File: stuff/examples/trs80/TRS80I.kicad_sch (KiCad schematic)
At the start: 74 parts, among them U5 4023, U6 4023

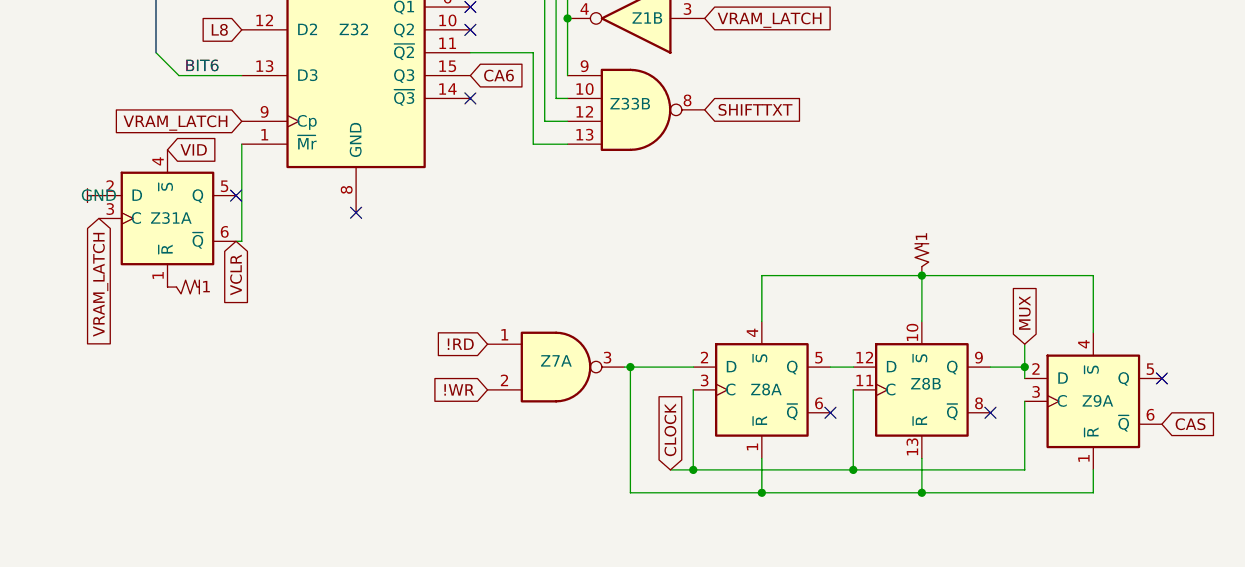
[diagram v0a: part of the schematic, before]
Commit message: Fis RS pins in DCTrigger Use Optimiser for DCTrigger pins in case of no R/S pins
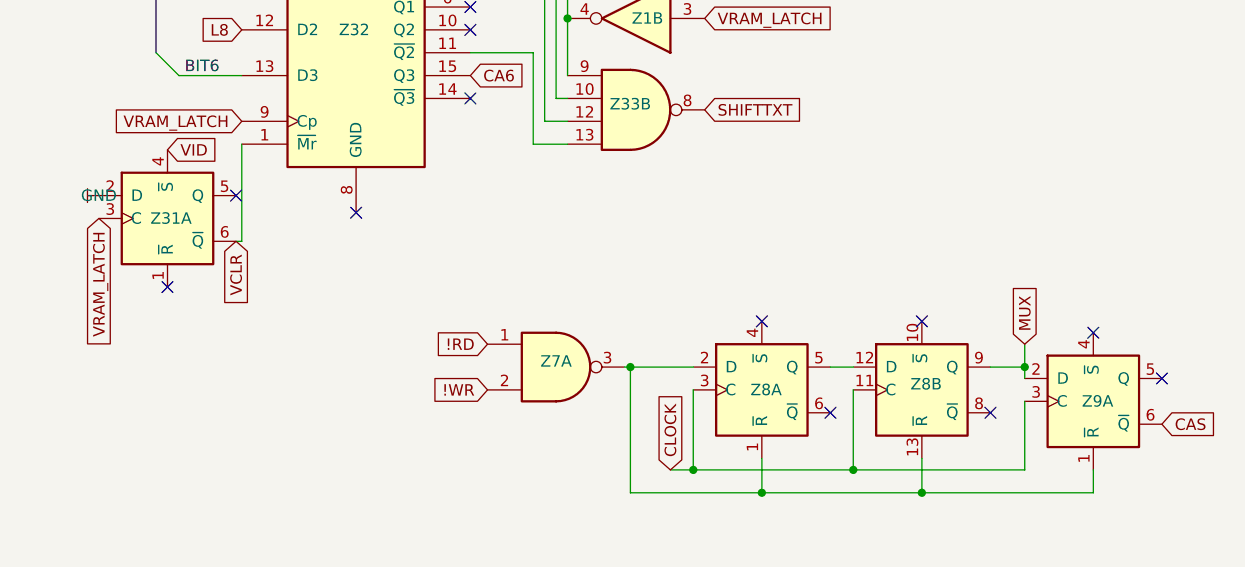
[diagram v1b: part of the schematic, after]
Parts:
- removed pullup30, pullup9: pull_up, symbol chip:PULLUP
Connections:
- now unconnected: Z8.10 (~{S}), Z8.4 (~{S}), Z9.4 (~{S})
- no-connect marks 35 -> 39
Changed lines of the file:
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@@
   (junction (at 292.735 90.17) (diameter 0) (color 0 0 0 0)
   )
-  (junction (at 333.375 122.555) (diameter 0) (color 0 0 0 0)
-  )
   (junction (at 333.375 146.685) (diameter 0) (color 0 0 0 0)
   )
@@
   (junction (at 259.715 45.72) (diameter 0) (color 0 0 0 0)
   )
+  (no_connect (at 249.555 123.825))
   (no_connect (at 203.2 62.865))
   (no_connect (at 193.04 260.985))
@@
   (no_connect (at 340.995 137.795))
   (no_connect (at 152.4 44.45))
+  (no_connect (at 333.375 127.635))
+  (no_connect (at 352.425 128.905))
   (no_connect (at 203.2 65.405))
   (no_connect (at 283.21 92.71))
@@
   (no_connect (at 168.91 71.12))
   (no_connect (at 115.57 90.805))
+  (no_connect (at 315.595 127.635))
   (no_connect (at 107.95 170.18))
   (no_connect (at 168.91 68.58))
@@
     (stroke (width 0) (type default))
   )
-  (wire (pts (xy 352.425 128.905) (xy 352.425 122.555))
-    (stroke (width 0) (type default))
-  )
   (bus (pts (xy 132.08 25.4) (xy 132.08 27.94))
     (stroke (width 0) (type default))
@@
     (stroke (width 0) (type default))
   )
-  (wire (pts (xy 333.375 122.555) (xy 352.425 122.555))
-    (stroke (width 0) (type default))
-  )
   (wire (pts (xy 223.52 45.085) (xy 226.695 45.085))
     (stroke (width 0) (type default))
@@
     (stroke (width 0) (type default))
   )
-  (wire (pts (xy 315.595 122.555) (xy 315.595 127.635))
-    (stroke (width 0) (type default))
-  )
   (wire (pts (xy 241.3 43.18) (xy 241.935 43.18))
     (stroke (width 0) (type default))
@@
     (stroke (width 0) (type default))
   )
-  (wire (pts (xy 333.375 122.555) (xy 333.375 127.635))
-    (stroke (width 0) (type default))
-  )
   (wire (pts (xy 147.955 191.135) (xy 151.765 191.135))
     (stroke (width 0) (type default))
@@
     (stroke (width 0) (type default))
   )
-  (wire (pts (xy 315.595 122.555) (xy 333.375 122.555))
-    (stroke (width 0) (type default))
-  )
   (bus (pts (xy 231.775 30.48) (xy 231.775 57.15))
     (stroke (width 0) (type default))
@@
     )
   )
-  (symbol (lib_id "chip:PULLUP") (at 249.555 123.825 180) (unit 1)
-    (in_bom yes) (on_board yes) (dnp no)
-    (property "Reference" "pullup30" (at 249.555 121.285 0)
-      (effects (font (size 1.27 1.27)) hide)
-    )
-    (property "Value" "pull_up" (at 249.555 121.285 0)
-      (effects (font (size 1.27 1.27)) hide)
-    )
-    (property "Footprint" "" (at 249.555 123.825 0)
-      (effects (font (size 1.27 1.27)) hide)
-    )
-    (property "Datasheet" "" (at 249.555 123.825 0)
-      (effects (font (size 1.27 1.27)) hide)
-    )
-    (pin "1")
-    (instances
-      (project "TRS80I"
-        (path "/5810480a-4982-4194-abfa-f24d4210ea86"
-          (reference "pullup30") (unit 1)
-        )
-      )
-    )
-  )
   (symbol (lib_id "chip:PULLUP") (at 259.715 29.21 0) (mirror x) (unit 1)
     (in_bom yes) (on_board yes) (dnp no)
@@
         )
       )
-    )
-  )
-  (symbol (lib_id "chip:PULLUP") (at 333.375 122.555 270) (unit 1)
-    (in_bom yes) (on_board yes) (dnp no)
-    (property "Reference" "pullup9" (at 330.835 122.555 0)
-      (effects (font (size 1.27 1.27)) hide)
-    )
-    (property "Value" "pull_up" (at 330.835 122.555 0)
-      (effects (font (size 1.27 1.27)) hide)
-    )
-    (property "Footprint" "" (at 333.375 122.555 0)
-      (effects (font (size 1.27 1.27)) hide)
-    )
-    (property "Datasheet" "" (at 333.375 122.555 0)
-      (effects (font (size 1.27 1.27)) hide)
-    )
-    (pin "1")
-    (instances
-      (project "TRS80I"
-        (path "/5810480a-4982-4194-abfa-f24d4210ea86"
-          (reference "pullup9") (unit 1)
-        )
-      )

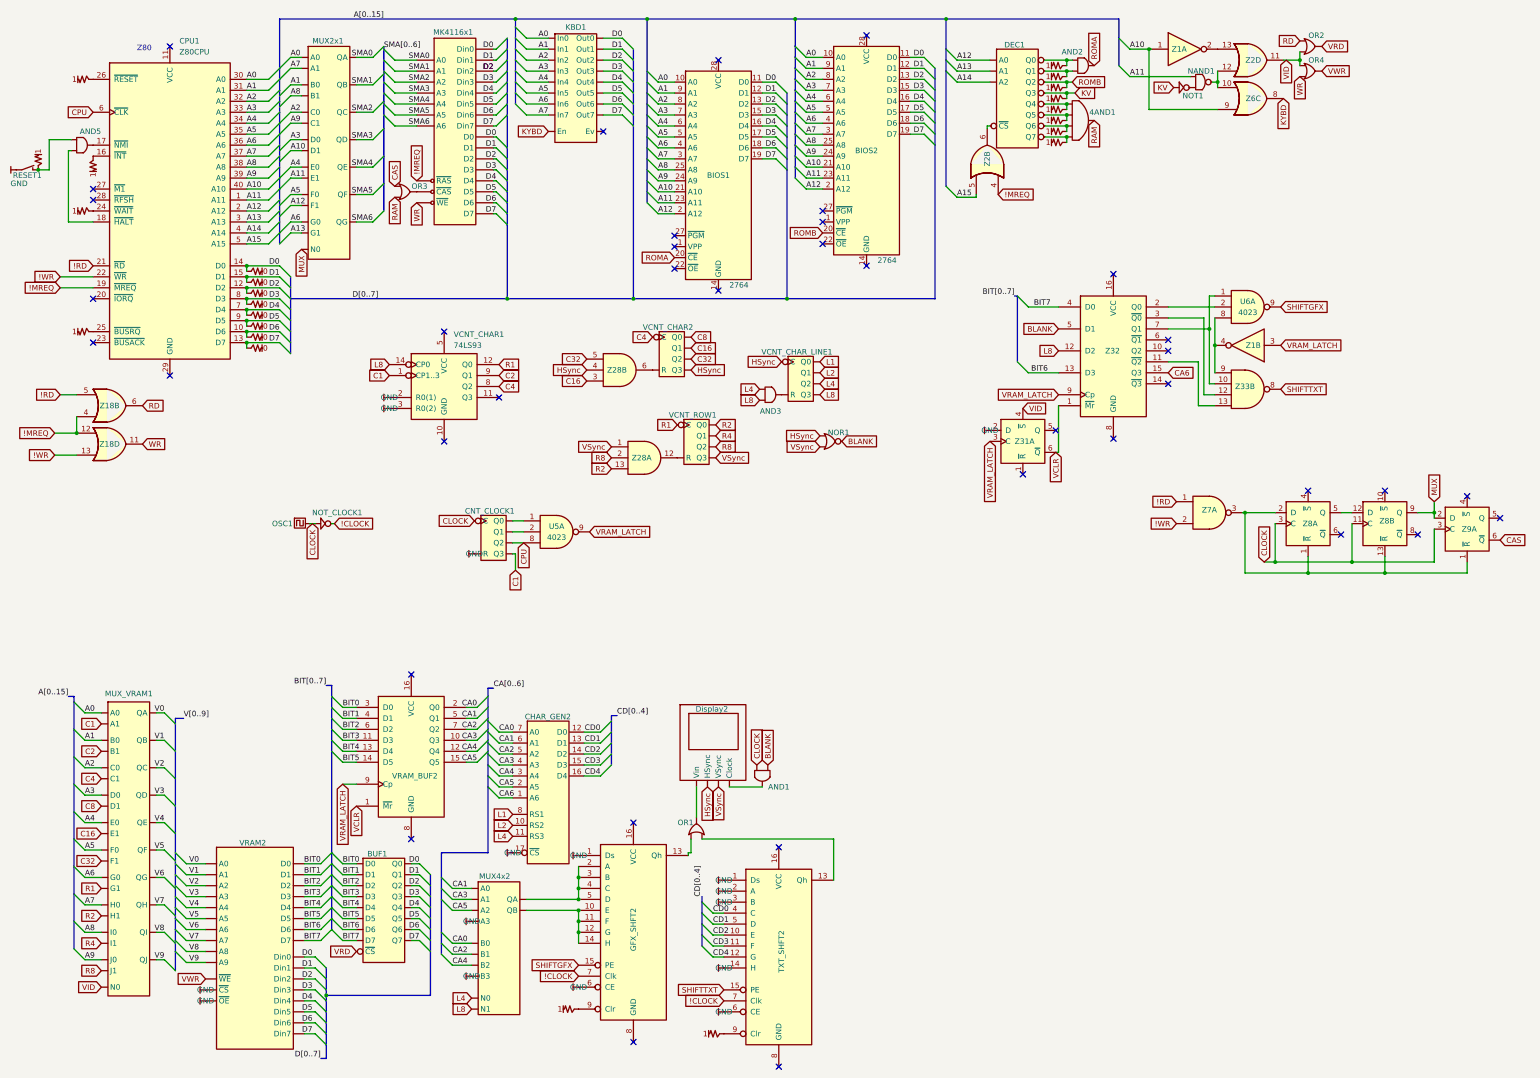
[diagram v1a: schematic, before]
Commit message: fix 74LS92 (It's not divider by 16, but rather by 12). Other fixes.
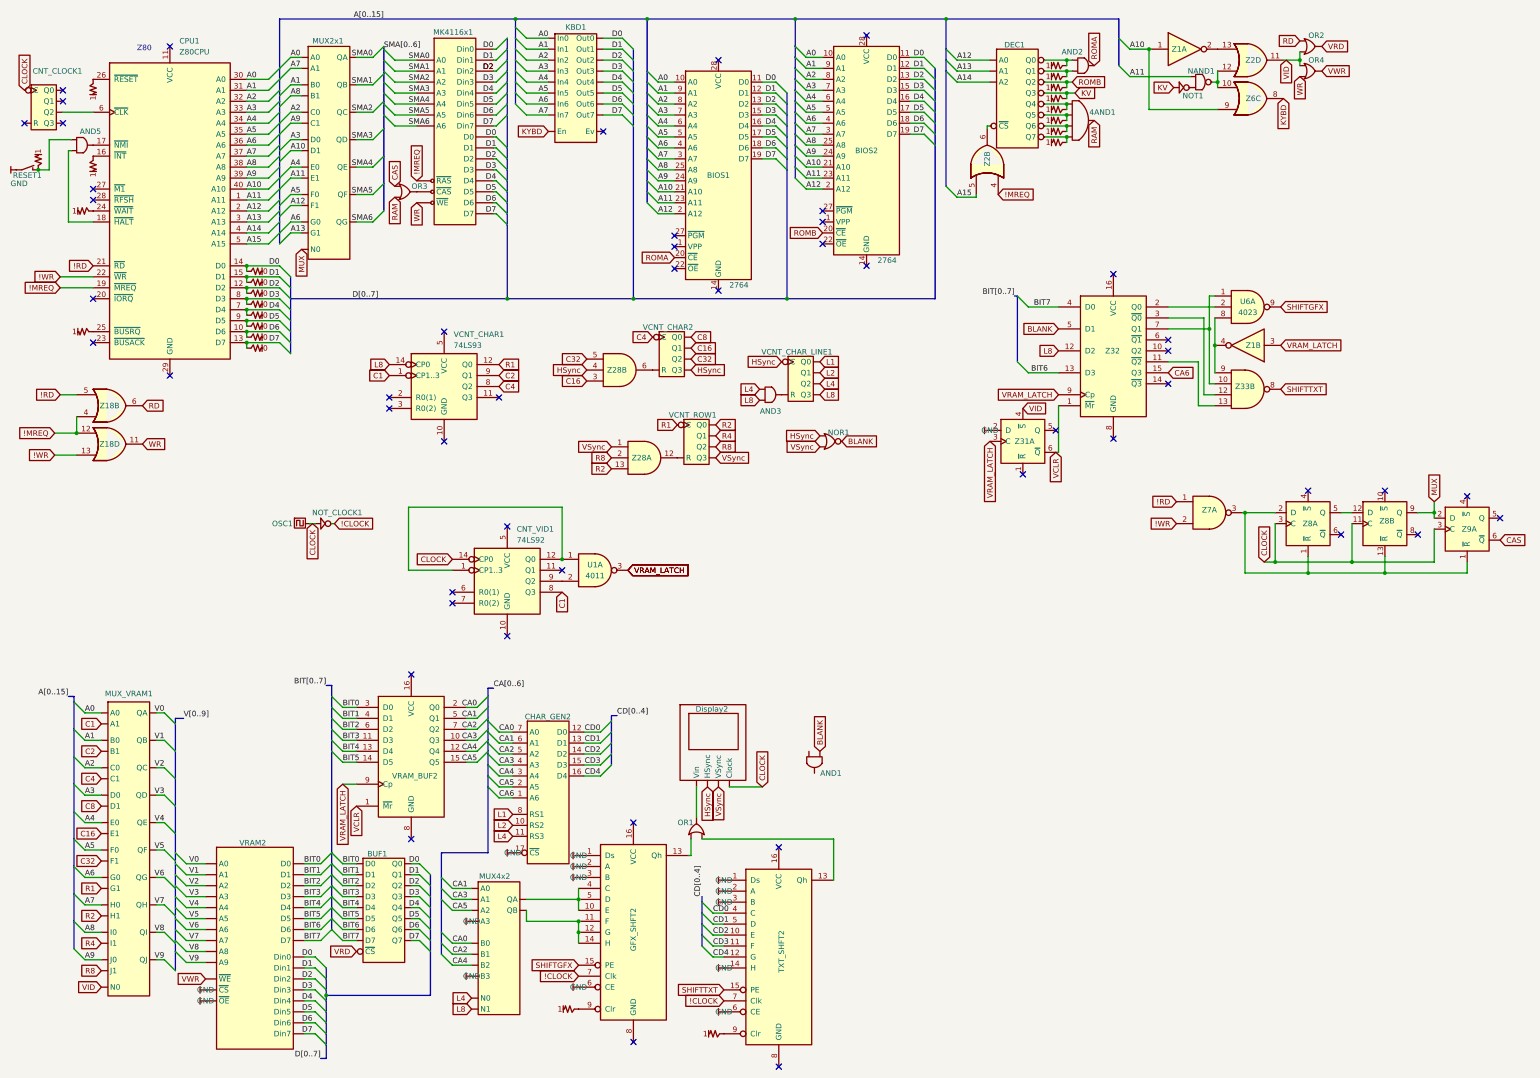
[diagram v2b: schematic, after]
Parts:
- removed U5: 4023, symbol 4xxx:4023
- added CNT_VID1: 74LS92, TRS80IUS:DIP-14_W7.62mm, symbol 74xx:74LS92
- added U1: 4011, symbol 4xxx:4011
- OSC1: SymPartParam start -> (none)
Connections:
- net C1: now also CNT_VID1.8 (Q3); no longer CNT_CLOCK1.5 (Q3)
- net CLOCK: now also Display2.1 (Clock), CNT_VID1.14 (CP0); no longer AND1.1 (IN0)
- net VRAM_LATCH: now also U1.3
- net gnd: now also GFX_SHFT2.2 (A), GFX_SHFT2.3 (B); no longer CNT_CLOCK1.1 (R), VCNT_CHAR1.2 (R0(1)), VCNT_CHAR1.3 (R0(2))
- net at AND1.3 (OUT): no longer Display2.1 (Clock)
- net at GFX_SHFT2.11 (F), GFX_SHFT2.12 (G), GFX_SHFT2.14 (H)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: no longer GFX_SHFT2.10 (E)
- net at GFX_SHFT2.4 (C), GFX_SHFT2.5 (D), MUX4x2.11 (QA): now also GFX_SHFT2.10 (E); no longer GFX_SHFT2.2 (A), GFX_SHFT2.3 (B)
- net CPU: no longer names the net of CNT_CLOCK1.4 (Q2), CPU1.6 (~{CLK})
- new net: CNT_VID1.1 (CP1..3), CNT_VID1.12 (Q0), U1.1
- new net: CNT_VID1.9 (Q2), U1.2
- no-connect marks 39 -> 50

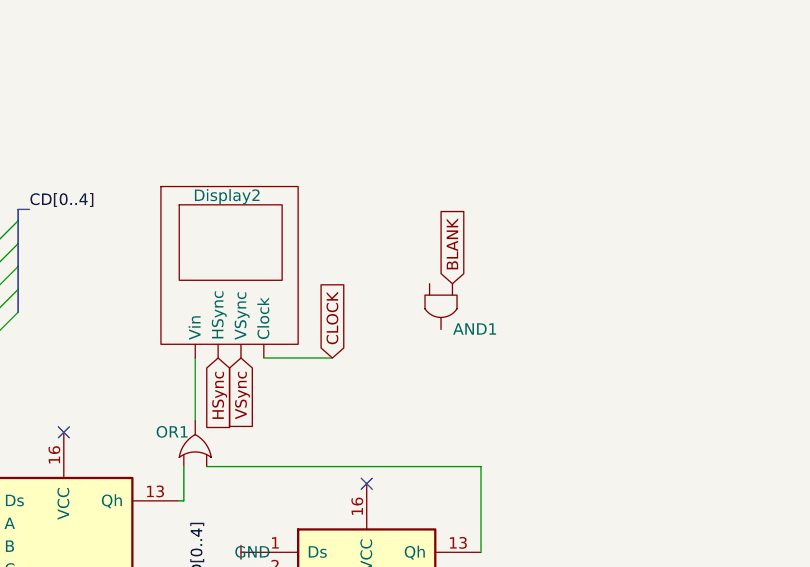
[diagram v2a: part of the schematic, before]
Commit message: Expand wire API
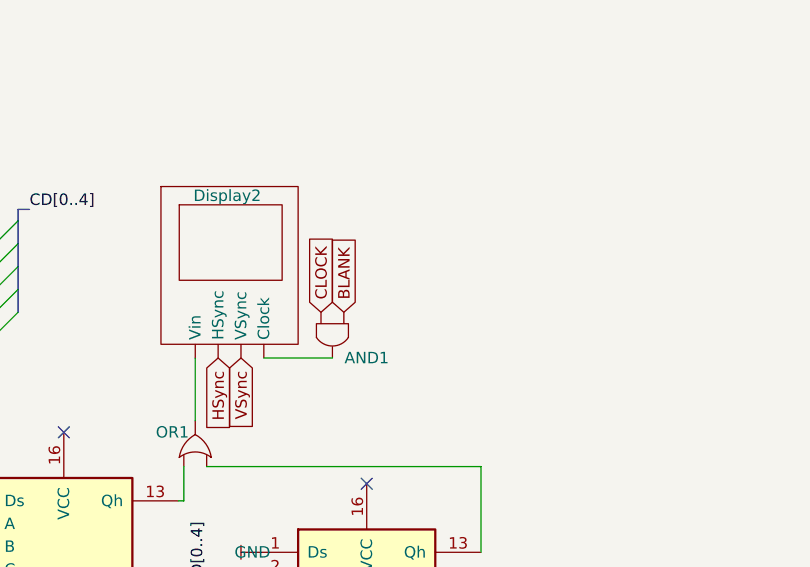
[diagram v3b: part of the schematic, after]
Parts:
- OSC1: SymPartParam (none) -> start
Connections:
- net CLOCK: now also AND1.1 (IN0); no longer Display2.1 (Clock)
- net at AND1.3 (OUT): now also Display2.1 (Clock)
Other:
- moved on the sheet: AND1
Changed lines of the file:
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@@
-    )
-  )
-  (global_label "CLOCK" (shape input) (at 189.23 196.215 90) (fields_autoplaced)
-    (effects (font (size 1.27 1.27)) (justify left))
-    (property "Intersheetrefs" "${INTERSHEET_REFS}" (at 189.23 188.0288 90)
-      (effects (font (size 1.27 1.27)) (justify right) hide)
     )
   )
@@
     )
   )
+  (global_label "CLOCK" (shape input) (at 187.96 191.135 90) (fields_autoplaced)
+    (effects (font (size 1.27 1.27)) (justify left))
+    (property "Intersheetrefs" "${INTERSHEET_REFS}" (at 187.96 182.9488 90)
+      (effects (font (size 1.27 1.27)) (justify right) hide)
+    )
+  )
   (global_label "SHIFTGFX" (shape input) (at 309.245 85.09 0) (fields_autoplaced)
     (effects (font (size 1.27 1.27)) (justify left))
@@
     )
   )
-  (global_label "BLANK" (shape input) (at 202.565 187.96 90) (fields_autoplaced)
-    (effects (font (size 1.27 1.27)) (justify left))
-    (property "Intersheetrefs" "${INTERSHEET_REFS}" (at 202.565 178.9876 90)
+  (global_label "BLANK" (shape input) (at 190.5 191.135 90) (fields_autoplaced)
+    (effects (font (size 1.27 1.27)) (justify left))
+    (property "Intersheetrefs" "${INTERSHEET_REFS}" (at 190.5 182.1626 90)
       (effects (font (size 1.27 1.27)) (justify left) hide)
     )
@@
       (effects (font (size 1.27 1.27)) hide)
     )
-    (property "SymPartParam" "" (at 84.455 135.255 0)
+    (property "SymPartParam" "start" (at 84.455 135.255 0)
       (effects (font (size 1.27 1.27)) hide)
     )
@@
     )
   )
-  (symbol (lib_id "chip:AND") (at 201.295 190.5 90) (mirror x) (unit 1)
-    (in_bom yes) (on_board yes) (dnp no)
-    (property "Reference" "AND1" (at 205.105 193.04 90)
-      (effects (font (size 1.27 1.27)))
-    )
-    (property "Value" "AND" (at 205.105 190.5 0)
-      (effects (font (size 1.27 1.27)) hide)
-    )
-    (property "Footprint" "" (at 203.835 190.5 0)
-      (effects (font (size 1.27 1.27)) hide)
-    )
-    (property "Datasheet" "" (at 203.835 190.5 0)
-      (effects (font (size 1.27 1.27)) hide)
-    )
+  (symbol (lib_id "chip:AND") (at 189.23 193.675 90) (mirror x) (unit 1)
+    (in_bom yes) (on_board yes) (dnp no)
+    (property "Reference" "AND1" (at 193.04 196.215 90)
+      (effects (font (size 1.27 1.27)))
+    )
+    (property "Value" "AND" (at 193.04 193.675 0)
+      (effects (font (size 1.27 1.27)) hide)
+    )
+    (property "Footprint" "" (at 191.77 193.675 0)
+      (effects (font (size 1.27 1.27)) hide)
+    )
+    (property "Datasheet" "" (at 191.77 193.675 0)
+      (effects (font (size 1.27 1.27)) hide)
+    )

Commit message: cleanup
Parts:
- BIOS1: SymPartParam file=rom_a_L2.bin -> (none)
- BIOS2: SymPartParam file=rom_b_L2.bin -> (none)
- CHAR_GEN2: SymPartParam file=character_set_10.bin -> (none)
- KBD1: SymPartParam map=Back Quote_00|A_01|B_02|C_03|D_04|E_05|F_06|G_07|H_10|I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 -> (none)
- OSC1: SymPartParam start -> (none)
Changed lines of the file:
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@@
-      (effects (font (size 1.27 1.27)) hide)
-    )
-    (property "SymPartParam" "map=Back Quote_00|A_01|B_02|C_03|D_04|E_05|F_06|G_07|H_10|I_11|J_12|K_13|L_14|M_15|N_16|O_17|P_20|Q_21|R_22|S_23|T_24|U_25|V_26|W_27|X_30|Y_31|Z_32|0_40|1_41|2_42|3_43|4_44|5_45|6_46|7_47|8_50|9_51|Semicolon_52|Quote_53|Comma_54|Minus_55|Period_56|Slash_57|Enter_60|Home_61|Escape_62|Up_63|Down_64|Left_65|Right_66|Space_67|Shift_70|Ctrl_74|Backspace_65" (at 146.05 34.29 0)
       (effects (font (size 1.27 1.27)) hide)
     )
@@
       (effects (font (size 1.27 1.27)) hide)
     )
-    (property "SymPartParam" "start" (at 84.455 135.255 0)
-      (effects (font (size 1.27 1.27)) hide)
-    )
     (pin "1")
     (instances
@@
     )
     (property "Datasheet" "https://www.datasheet.in/pdf-down/M/C/M/MCM6670_MotorolaSemiconductor.pdf" (at 133.803 224.917 0)
-      (effects (font (size 1.27 1.27)) hide)
-    )
-    (property "SymPartParam" "file=character_set_10.bin" (at 140.335 196.215 0)
       (effects (font (size 1.27 1.27)) hide)
     )
@@
       (effects (font (size 1.27 1.27)) hide)
     )
-    (property "SymPartParam" "file=rom_a_L2.bin" (at 179.07 53.34 0)
-      (effects (font (size 1.27 1.27)) hide)
-    )
     (pin "23")
     (pin "6")
@@
       (effects (font (size 1.27 1.27)) hide)
     )
-    (property "SymPartParam" "file=rom_b_L2.bin" (at 213.36 47.625 0)
-      (effects (font (size 1.27 1.27)) hide)
-    )
